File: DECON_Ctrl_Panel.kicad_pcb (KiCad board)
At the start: 2 copper layers, 174 x 105.4 mm, 274 parts, among them J1 Conn_01x02, J10 Conn_01x04, J11 Conn_01x06, J12 Conn_01x06, J13 Conn_01x04, J18 Conn_01x04, J3 Conn_01x06, J4 Conn_01x06, J5 FLASH, J6 Conn_01x06, J7 Conn_01x05, J8 Conn_01x06, J9 Conn_01x06, K1 G5NB, K10 G5NB, K11 G5NB, K12 G5NB, K13 G5NB, K14 G5NB, K15 G5NB, K16 G5NB, K17 G5NB, K2 G5NB, K3 G5NB, K4 G5NB, K5 G5NB, K6 G5NB, K7 G5NB, K8 G5NB, K9 G5NB, Q1 MMBT2222A, Q10 MMBT2222A, Q11 MMBT2222A, Q12 MMBT2222A, Q13 MMBT2222A, Q14 MMBT2222A, Q15 MMBT2222A, Q16 MMBT2222A, Q2 MMBT2222A, Q3 MMBT2222A, Q4 MMBT2222A, Q5 MMBT2222A, Q6 MMBT2222A, Q7 MMBT2222A, Q8 MMBT2222A, Q9 MMBT2222A, SW1 SW_Push, SW2 SW_Push, U1 URB2405YMD-10WR3, U10 LTV-817S, U11 LTV-817S, U12 LTV-817S, U13 LTV-817S, U14 LTV-817S, U15 LTV-817S, U16 LTV-817S, U17 LTV-817S, U18 LTV-817S, U19 LTV-817S, U2 AZ1117-3.3, U20 74HC138, U21 LTV-817S, U22 LTV-817S, U23 LTV-817S, U24 LTV-817S, U25 LTV-817S, U26 LTV-817S, U27 LTV-817S, U28 LTV-817S, U29 LTV-817S, U3 STM32F401R_B-C_Tx, U30 LTV-817S, U31 LTV-817S, U32 LTV-817S, U33 LTV-817S, U34 LTV-817S, U35 LTV-817S, U36 LTV-817S, U4 LTV-817S, U5 LTV-817S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

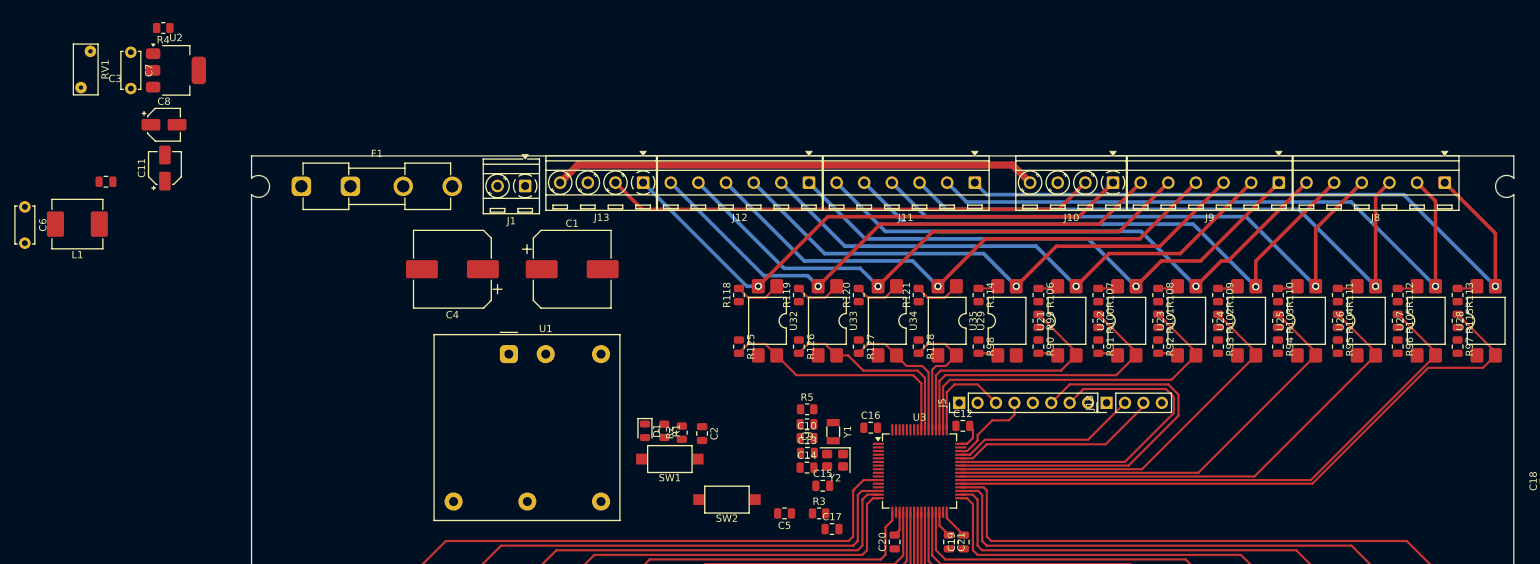
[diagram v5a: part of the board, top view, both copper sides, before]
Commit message: modified:   DECON_Ctrl_Panel.kicad_pcb 	modified:   DECON_Ctrl_Panel.kicad_prl 	modified:   decon_mcu.kicad_sch
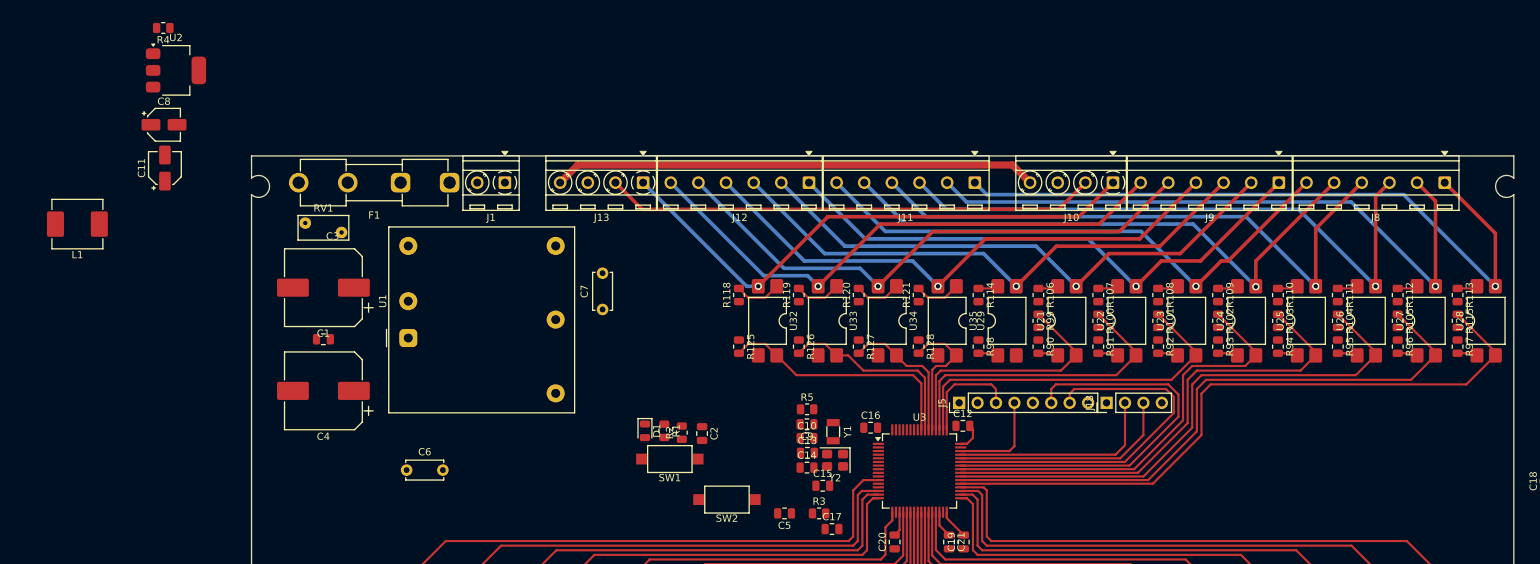
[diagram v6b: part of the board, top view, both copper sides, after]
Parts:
- moved C7 74.1 mm to (141.1, 74.5), turned to 90 degrees
- moved C6 63.9 mm to (114.1, 96.6), turned to 0 degrees
- moved RV1 41.1 mm to (105.1, 63.9), turned to 180 degrees
- moved C3 37.0 mm to (102.6, 78.6)
- moved C1 34.4 mm to (102.6, 71.5), turned to 180 degrees
- moved C4 24.4 mm to (102.6, 85.7)
- moved F1 20.4 mm to (120.0, 57.0), turned to 180 degrees
- moved U1 14.0 mm to (114.3, 78.4), turned to 90 degrees
- moved J1 2.83 mm to (127.6, 57.0)
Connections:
- J1 pad 1: VBAT -> GND_VBAT
- J1 pad 2: GND_VBAT -> VBAT
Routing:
- net 74138_Y3: track 55.0 -> 58.7 mm
- net 74138_Y4: track 63.5 -> 67.0 mm
- net 74138_Y5: track 71.9 -> 75.4 mm
- net 74138_Y6: track 80.4 -> 83.8 mm
- net MCD_D+: track 25.6 -> 29.0 mm
- net 74138_Y7: track 88.9 -> 92.2 mm
- net Net-(R97-Pad2): track 0.00 -> 2.79 mm
- net Net-(R94-Pad2): track 0.00 -> 2.79 mm
- net Net-(R93-Pad2): track 0.00 -> 2.79 mm
- net Net-(R96-Pad2): track 0.00 -> 2.79 mm
- net Net-(R95-Pad2): track 0.00 -> 2.79 mm
- net MCD_D-: track 28.7 -> 31.0 mm
- net PA13: track 11.6 -> 13.7 mm
- net MCU_TX1: track 54.9 -> 56.1 mm
- net PA14: track 13.2 -> 14.0 mm
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
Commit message: modified:   DECON_Ctrl_Panel.kicad_pcb 	modified:   DECON_Ctrl_Panel.kicad_prl 	modified:   decon_mcu.kicad_sch 	modified:   fp-info-cache
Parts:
- removed C18: 104, Capacitor_SMD:C_0805_2012Metric
- removed R87, R88, R89: 10K, Resistor_SMD:R_0805_2012Metric
- removed U20: 74HC138, Package_SO:SOIC-16_3.9x9.9mm_P1.27mm
- added D35: LED, LED_SMD:LED_0805_2012Metric, F.Cu at (172.5, 103.8)
- added J2: Conn_01x06, Connector_PinHeader_2.54mm:PinHeader_1x06_P2.54mm_Vertical, F.Cu at (158.1, 95.0)
- added R30: 1K, Resistor_SMD:R_0805_2012Metric, F.Cu at (172.5, 100.2)
- moved D2 78.8 mm to (141.5, 64.2), turned to -90 degrees
- moved R4 68.8 mm to (141.5, 67.6), turned to 90 degrees
- moved C11 56.4 mm to (136.1, 65.9)
- moved U2 51.9 mm to (128.1, 65.9), turned to -90 degrees
- moved C8 42.9 mm to (120.1, 65.9), turned to 90 degrees
- moved L1 42.1 mm to (104.5, 84.8), turned to -90 degrees
- moved C7 32.3 mm to (110.4, 64.4), turned to 0 degrees
- moved D1 26.2 mm to (169.9, 103.8), turned to 90 degrees
- moved R1 22.2 mm to (169.9, 100.2)
- moved R2 17.7 mm to (167.4, 100.2), turned to -90 degrees
- moved C2 17.5 mm to (167.4, 103.8)
- moved C17 15.1 mm to (177.7, 90.6)
- moved SW1 12.8 mm to (161.7, 101.2), turned to 90 degrees
- moved C4 10.2 mm to (102.6, 95.9)
- moved R5 8.33 mm to (161.0, 89.4), turned to 90 degrees
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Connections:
- C2 pad 1: 74138_Y3 -> BUILTIN_BTN
- D1 pad 1: PC13 -> BUILTIN_LED_1
- R2 pad 2: 74138_Y3 -> BUILTIN_BTN
- SW1 pad 1: 74138_Y3 -> BUILTIN_BTN
- U3 pad 10: PC2 -> BUILTIN_LED_0
- U3 pad 8: PC0 -> BUILTIN_BTN
- U3 pad 9: PC1 -> BUILTIN_LED_1
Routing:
- net 3.3V: track 11.4 -> 561.8 mm, vias 0 -> 70
- net 5V: track 0.00 -> 56.1 mm
- net Net-(C1-Pad1): track 0.00 -> 38.4 mm, vias 0 -> 3
- net PB8: track 0.00 -> 34.6 mm
- net PB5: track 0.00 -> 33.4 mm
- net PB9: track 0.00 -> 32.6 mm
- net PB6: track 0.00 -> 32.4 mm
- net PB7: track 0.00 -> 32.0 mm
- net PC13: track 0.00 -> 30.8 mm
- net NRST: track 0.00 -> 29.9 mm
- net BOOT0: track 0.00 -> 29.5 mm
- net BUILTIN_BTN: track 0.00 -> 25.3 mm
- net VBAT: track 100.5 -> 122.5 mm
- net Net-(U1-+VIN): track 0.00 -> 21.5 mm
- net OSC32_IN: track 0.00 -> 18.1 mm
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
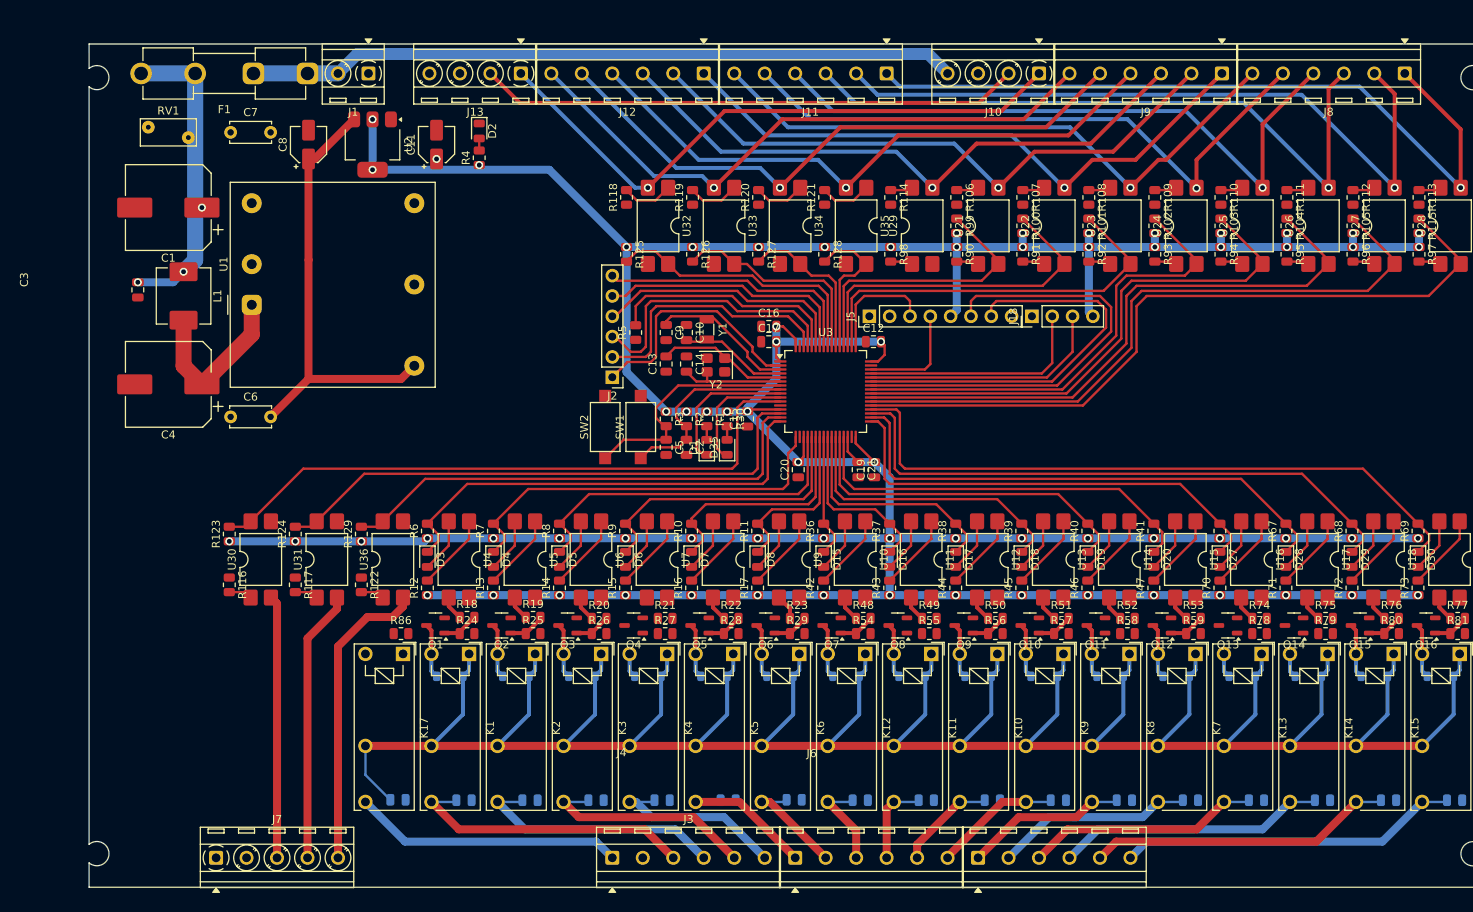
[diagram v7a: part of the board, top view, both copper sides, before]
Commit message: modified:   DECON_Ctrl_Panel.kicad_pcb 	modified:   DECON_Ctrl_Panel.kicad_prl 	modified:   decon_mcu.kicad_sch
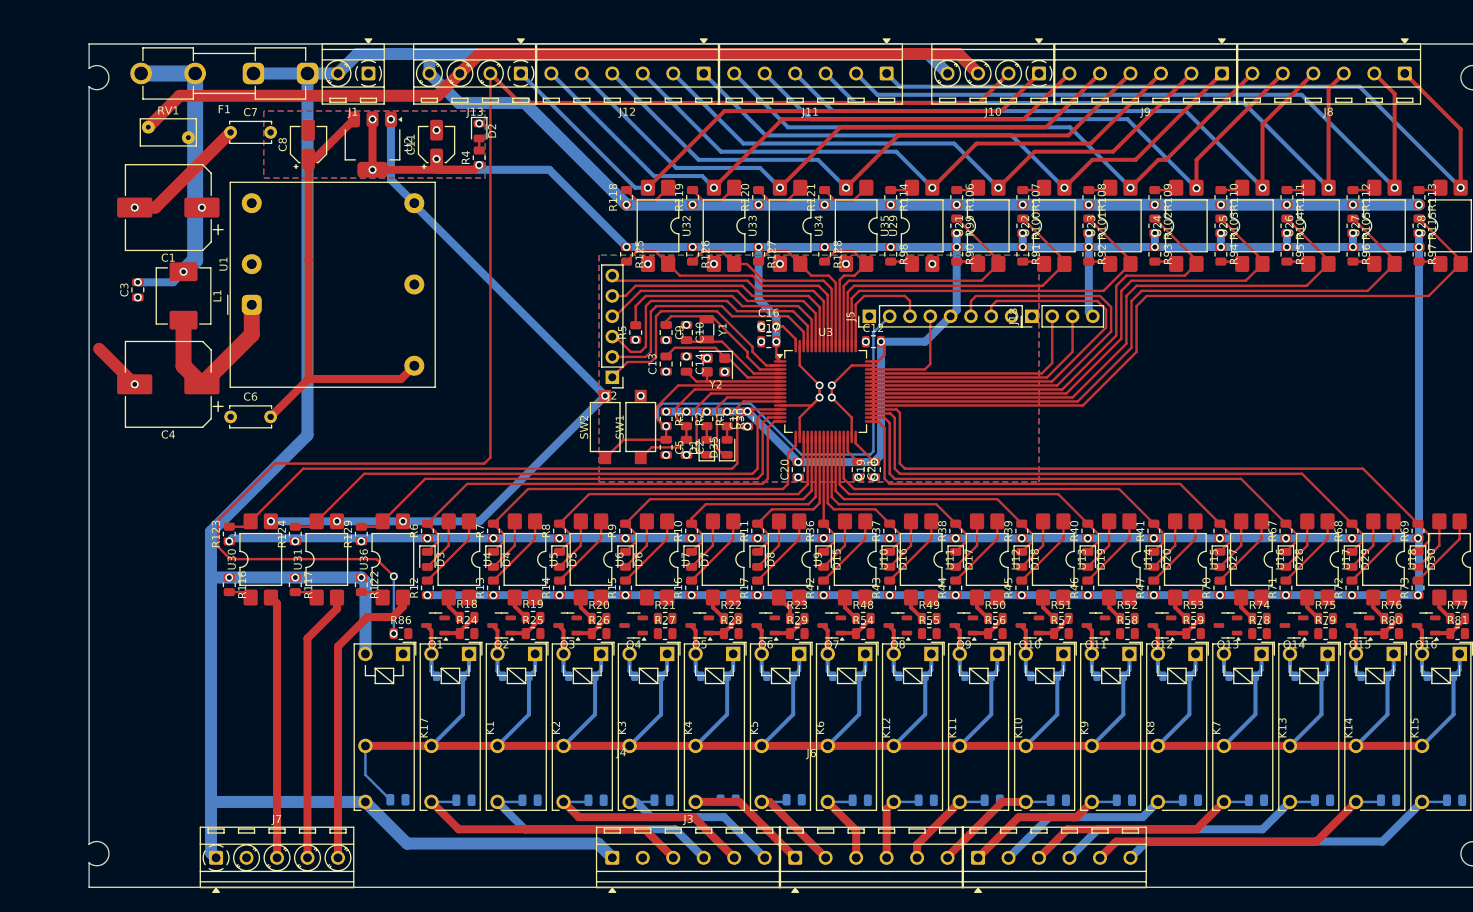
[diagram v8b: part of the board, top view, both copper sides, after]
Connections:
- C1 pad 2: GND_VBATT -> GND_VBAT
- C3 pad 2: GND_VBATT -> GND_VBAT
- C4 pad 2: GND_VBATT -> GND_VBAT
- C7 pad 1: GND_VBATT -> GND_VBAT
- RV1 pad 2: GND_VBATT -> GND_VBAT
- U1 pad 1: GND_VBATT -> GND_VBAT
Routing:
- net VBAT: track 122.5 -> 406.7 mm, vias 0 -> 16
- net GND_VBAT: track 0.00 -> 131.1 mm, vias 0 -> 3
- net GND_MCU: track 0.00 -> 126.1 mm, vias 0 -> 33
- net BUTTON_EN: track 67.8 -> 187.0 mm, vias 0 -> 2
- net NRST: track 29.9 -> 80.4 mm, vias 0 -> 1
- net 3.3V: track 561.8 -> 585.2 mm
- added copper zone on B.Cu, net GND_MCU
- added copper zone on F.Cu, net GND_MCU
